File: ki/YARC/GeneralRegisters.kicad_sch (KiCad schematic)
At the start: 0 parts

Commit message: Ongoing development of registers and ALU
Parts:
- added U? (x8): 74LS670, symbol 74xx:74LS670
- added U? (x4): 74LS157, symbol 74xx:74LS157
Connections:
- new net: U?.16 (VCC), U?.16 (VCC), U?.16 (VCC)
- new net: U?.8 (GND), U?.8 (GND), U?.8 (GND)
- new net 333: U?.12 (~{Ew})
- new net 4444: U?.11 (~{Er})
- new net 55555: U?.4 (Rb)
- new net ALUOUT15: U?.14 (I0d)
- new net DW.15: U?.3 (D4)
- new net SRC2.15: U?.6 (Q4)
- new net SYSDATA15: U?.13 (I1d)
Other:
- note added: "REGISTER BANK 1"
- note added: "REGISTER BANK 2"
- note added: "REGISTER INPUT MUX"

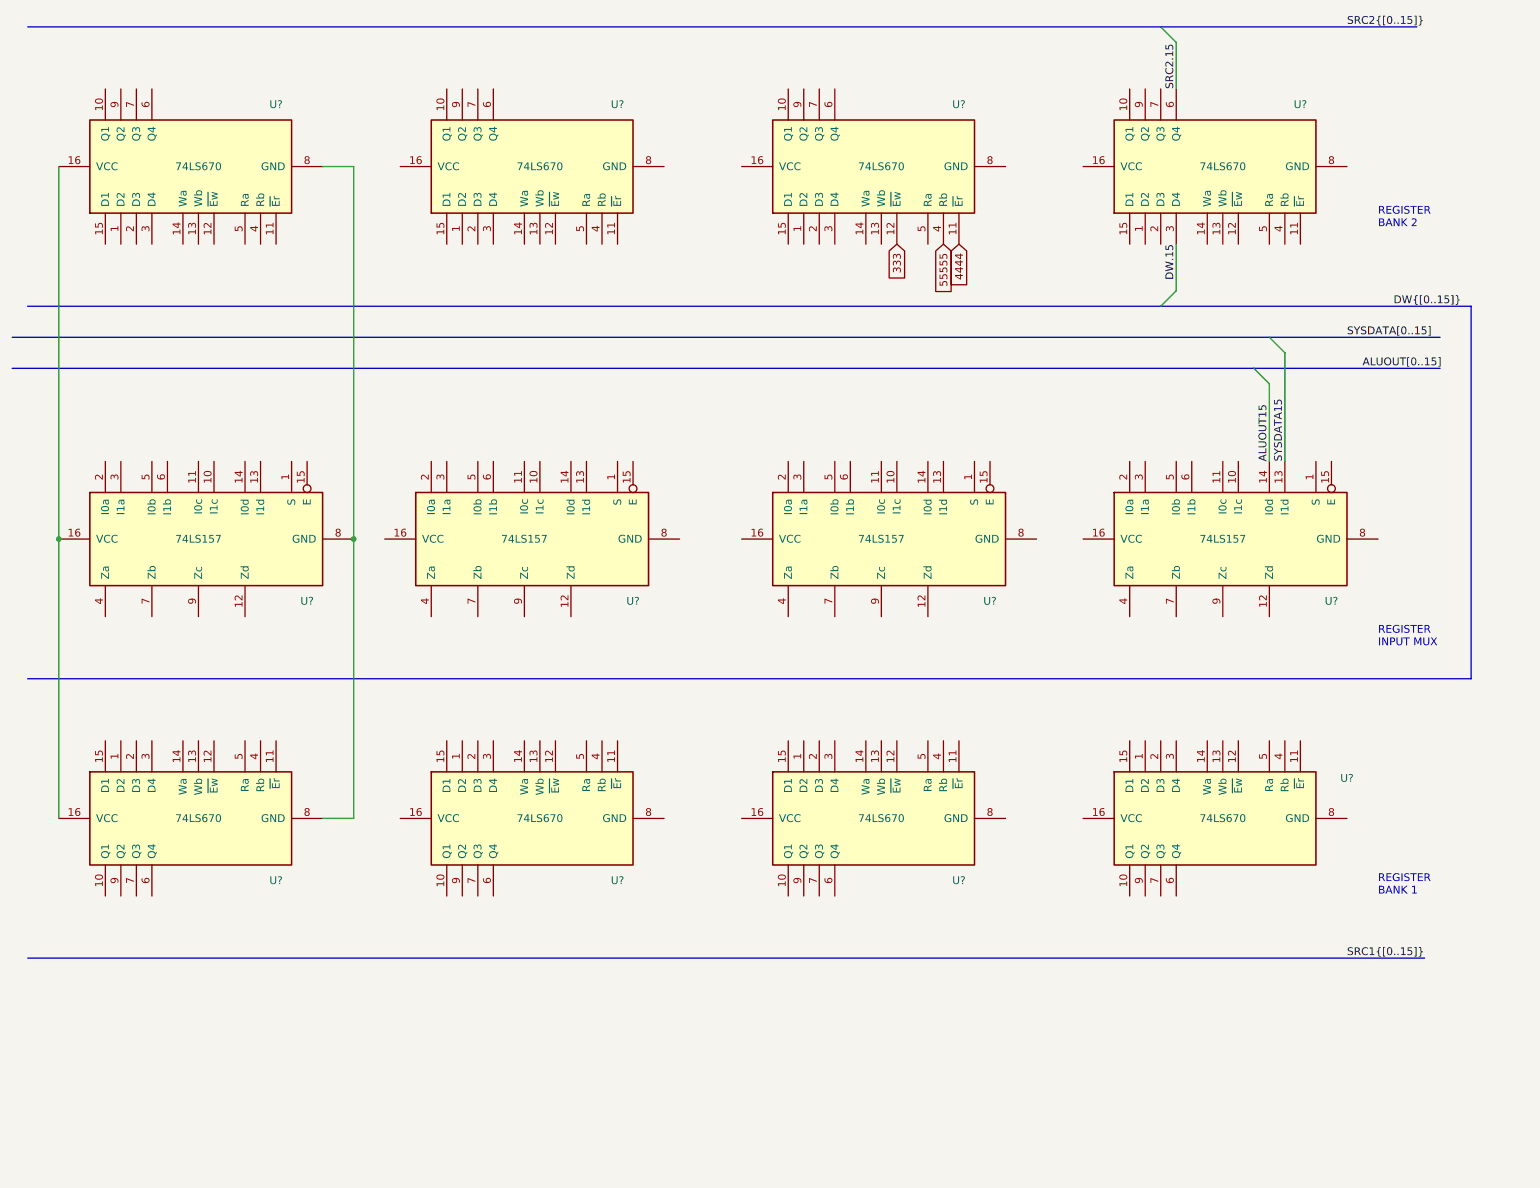
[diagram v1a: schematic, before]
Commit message: Expand ucode RAM test to 4 slices. Much work in KiCad.
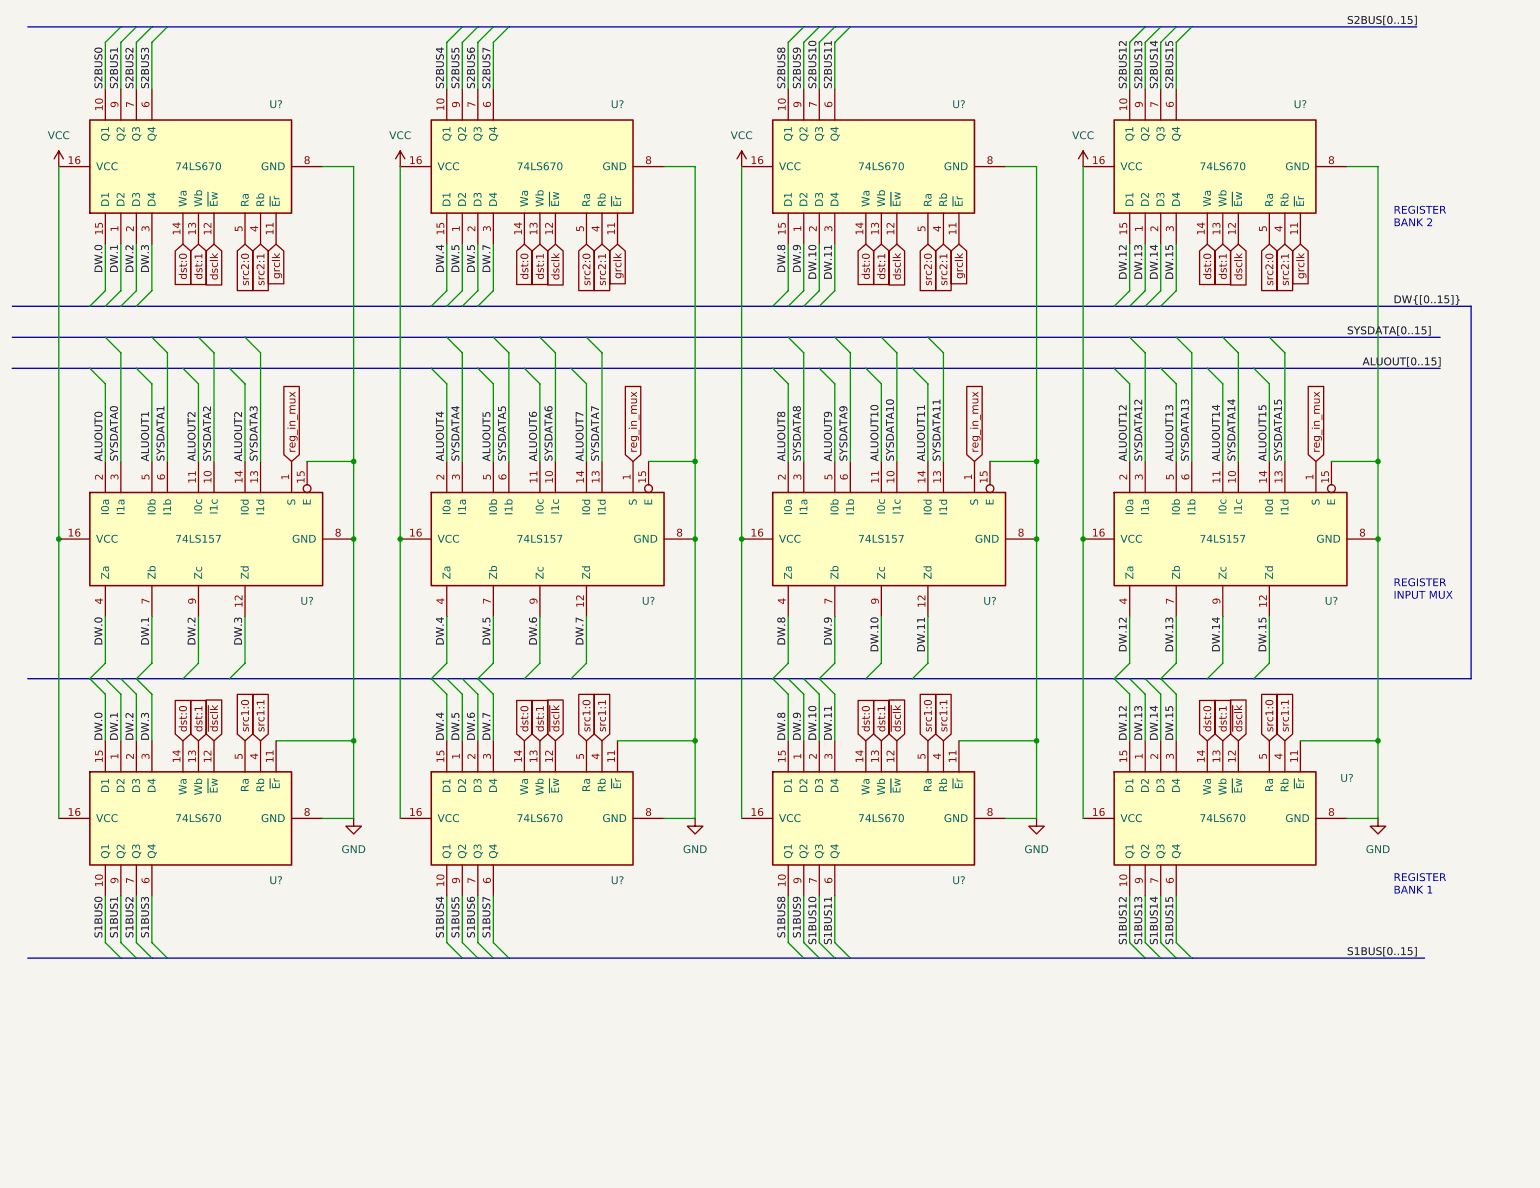
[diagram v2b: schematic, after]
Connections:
- net 333 is gone; now on net dsclk: U?.12 (~{Ew})
- net 4444 is gone; now on net grclk: U?.11 (~{Er})
- net 55555 is gone; now on net src2:1: U?.4 (Rb)
- net DW.15: now also U?.12 (Zd), U?.3 (D4)
- net DW.9: now reaches U?.1 (D2)
- net DW.9: now also U?.1 (D2), U?.7 (Zb)
- net S1BUS8: now reaches U?.10 (Q1)
- net GND: now reaches U?.11 (~{Er})
- net GND: now also U?.11 (~{Er}), U?.11 (~{Er}), U?.11 (~{Er}), U?.15 (E), U?.15 (E), U?.15 (E), U?.15 (E), U?.8 (GND), U?.8 (GND), U?.8 (GND), U?.8 (GND), U?.8 (GND), U?.8 (GND), U?.8 (GND), U?.8 (GND), U?.8 (GND), U?.8 (GND), U?.8 (GND), U?.8 (GND)
- net ~{dsclk}: now reaches U?.12 (~{Ew})
- net ~{dsclk}: now also U?.12 (~{Ew}), U?.12 (~{Ew}), U?.12 (~{Ew})
- net dst:1: now reaches U?.13 (Wb)
- net dst:1: now also U?.13 (Wb), U?.13 (Wb), U?.13 (Wb), U?.13 (Wb), U?.13 (Wb), U?.13 (Wb), U?.13 (Wb)
- net dst:0: now reaches U?.14 (Wa)
- net dst:0: now also U?.14 (Wa), U?.14 (Wa), U?.14 (Wa), U?.14 (Wa), U?.14 (Wa), U?.14 (Wa), U?.14 (Wa)
- net DW.8: now reaches U?.15 (D1)
- net DW.8: now also U?.15 (D1), U?.4 (Za)
- net VCC: now reaches U?.16 (VCC)
- net VCC: now also U?.16 (VCC), U?.16 (VCC), U?.16 (VCC), U?.16 (VCC), U?.16 (VCC), U?.16 (VCC), U?.16 (VCC), U?.16 (VCC), U?.16 (VCC), U?.16 (VCC), U?.16 (VCC)
- net DW.10: now reaches U?.2 (D3)
- net DW.10: now also U?.2 (D3), U?.9 (Zc)
- net DW.11: now reaches U?.3 (D4)
- net DW.11: now also U?.12 (Zd), U?.3 (D4)
- net src1:1: now reaches U?.4 (Rb)
- net src1:1: now also U?.4 (Rb), U?.4 (Rb), U?.4 (Rb)
- net src1:0: now reaches U?.5 (Ra)
- net src1:0: now also U?.5 (Ra), U?.5 (Ra), U?.5 (Ra)
- net S1BUS11: now reaches U?.6 (Q4)
- net S1BUS10: now reaches U?.7 (Q3)
- net S1BUS9: now reaches U?.9 (Q2)
- net DW.13: now reaches U?.1 (D2)
- net DW.13: now also U?.1 (D2), U?.7 (Zb)
- net S1BUS12: now reaches U?.10 (Q1)
- net DW.12: now reaches U?.15 (D1)
- net DW.12: now also U?.15 (D1), U?.4 (Za)
- net DW.14: now reaches U?.2 (D3)
- net DW.14: now also U?.2 (D3), U?.9 (Zc)
- net S1BUS15: now reaches U?.6 (Q4)
- net S1BUS14: now reaches U?.7 (Q3)
- net S1BUS13: now reaches U?.9 (Q2)
- net DW.5: now reaches U?.1 (D2)
- net DW.5: now also U?.1 (D2), U?.2 (D3), U?.7 (Zb)
- net S2BUS4: now reaches U?.10 (Q1)
- net grclk: now reaches U?.11 (~{Er})
- net grclk: now also U?.11 (~{Er}), U?.11 (~{Er})
- net dsclk: now reaches U?.12 (~{Ew})
- net dsclk: now also U?.12 (~{Ew}), U?.12 (~{Ew})
- net DW.4: now reaches U?.15 (D1)
- net DW.4: now also U?.15 (D1), U?.4 (Za)
- net DW.7: now reaches U?.3 (D4)
- net DW.7: now also U?.12 (Zd), U?.3 (D4)
- net src2:1: now reaches U?.4 (Rb)
- net src2:1: now also U?.4 (Rb), U?.4 (Rb)
- net src2:0: now reaches U?.5 (Ra)
- net src2:0: now also U?.5 (Ra), U?.5 (Ra), U?.5 (Ra)
- net S2BUS7: now reaches U?.6 (Q4)
- net S2BUS6: now reaches U?.7 (Q3)
- net S2BUS5: now reaches U?.9 (Q2)
- net reg_in_mux: now reaches U?.1 (S)
- net reg_in_mux: now also U?.1 (S), U?.1 (S), U?.1 (S)
- net SYSDATA10: now reaches U?.10 (I1c)
- net ALUOUT10: now reaches U?.11 (I0c)
- net SYSDATA11: now reaches U?.13 (I1d)
- net ALUOUT11: now reaches U?.14 (I0d)
- net ALUOUT8: now reaches U?.2 (I0a)
- net SYSDATA8: now reaches U?.3 (I1a)
- net ALUOUT9: now reaches U?.5 (I0b)
- net SYSDATA9: now reaches U?.6 (I1b)
- net SYSDATA2: now reaches U?.10 (I1c)
- net ALUOUT2: now reaches U?.11 (I0c)
- net ALUOUT2: now also U?.14 (I0d)
- net DW.3: now reaches U?.12 (Zd)
- net DW.3: now also U?.3 (D4), U?.3 (D4)
- net SYSDATA3: now reaches U?.13 (I1d)
- net ALUOUT0: now reaches U?.2 (I0a)
- net SYSDATA0: now reaches U?.3 (I1a)
- net DW.0: now reaches U?.4 (Za)
- net DW.0: now also U?.15 (D1), U?.15 (D1)
- net ALUOUT1: now reaches U?.5 (I0b)
- net SYSDATA1: now reaches U?.6 (I1b)
- net DW.1: now reaches U?.7 (Zb)
- net DW.1: now also U?.1 (D2), U?.1 (D2)
- net DW.2: now reaches U?.9 (Zc)
- net DW.2: now also U?.2 (D3), U?.2 (D3)
- net S2BUS12: now reaches U?.10 (Q1)
- net S2BUS14: now reaches U?.7 (Q3)
- net S2BUS13: now reaches U?.9 (Q2)
- net S1BUS0: now reaches U?.10 (Q1)
- net S1BUS3: now reaches U?.6 (Q4)
- net S1BUS2: now reaches U?.7 (Q3)
- net S1BUS1: now reaches U?.9 (Q2)
- net S1BUS4: now reaches U?.10 (Q1)
- net DW.6: now reaches U?.2 (D3)
- net DW.6: now also U?.9 (Zc)
- net S1BUS7: now reaches U?.6 (Q4)
- net S1BUS6: now reaches U?.7 (Q3)
- net S1BUS5: now reaches U?.9 (Q2)
- net SYSDATA6: now reaches U?.10 (I1c)
- net ALUOUT6: now reaches U?.11 (I0c)
- net SYSDATA7: now reaches U?.13 (I1d)
- net ALUOUT7: now reaches U?.14 (I0d)
- net ALUOUT4: now reaches U?.2 (I0a)
- net SYSDATA4: now reaches U?.3 (I1a)
- net ALUOUT5: now reaches U?.5 (I0b)
- net SYSDATA5: now reaches U?.6 (I1b)
- net S2BUS8: now reaches U?.10 (Q1)
- net S2BUS11: now reaches U?.6 (Q4)
- net S2BUS10: now reaches U?.7 (Q3)
- net S2BUS9: now reaches U?.9 (Q2)
- net S2BUS0: now reaches U?.10 (Q1)
- net S2BUS3: now reaches U?.6 (Q4)
- net S2BUS2: now reaches U?.7 (Q3)
- net S2BUS1: now reaches U?.9 (Q2)
- net SYSDATA14: now reaches U?.10 (I1c)
- net ALUOUT14: now reaches U?.11 (I0c)
- net ALUOUT12: now reaches U?.2 (I0a)
- net SYSDATA12: now reaches U?.3 (I1a)
- net ALUOUT13: now reaches U?.5 (I0b)
- net SYSDATA13: now reaches U?.6 (I1b)
- net SRC2.15 renamed S2BUS15
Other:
- moved on the sheet: U?

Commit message: Assign part labels (U-numbers) in KiCad and start adding them to Fritzing layouts
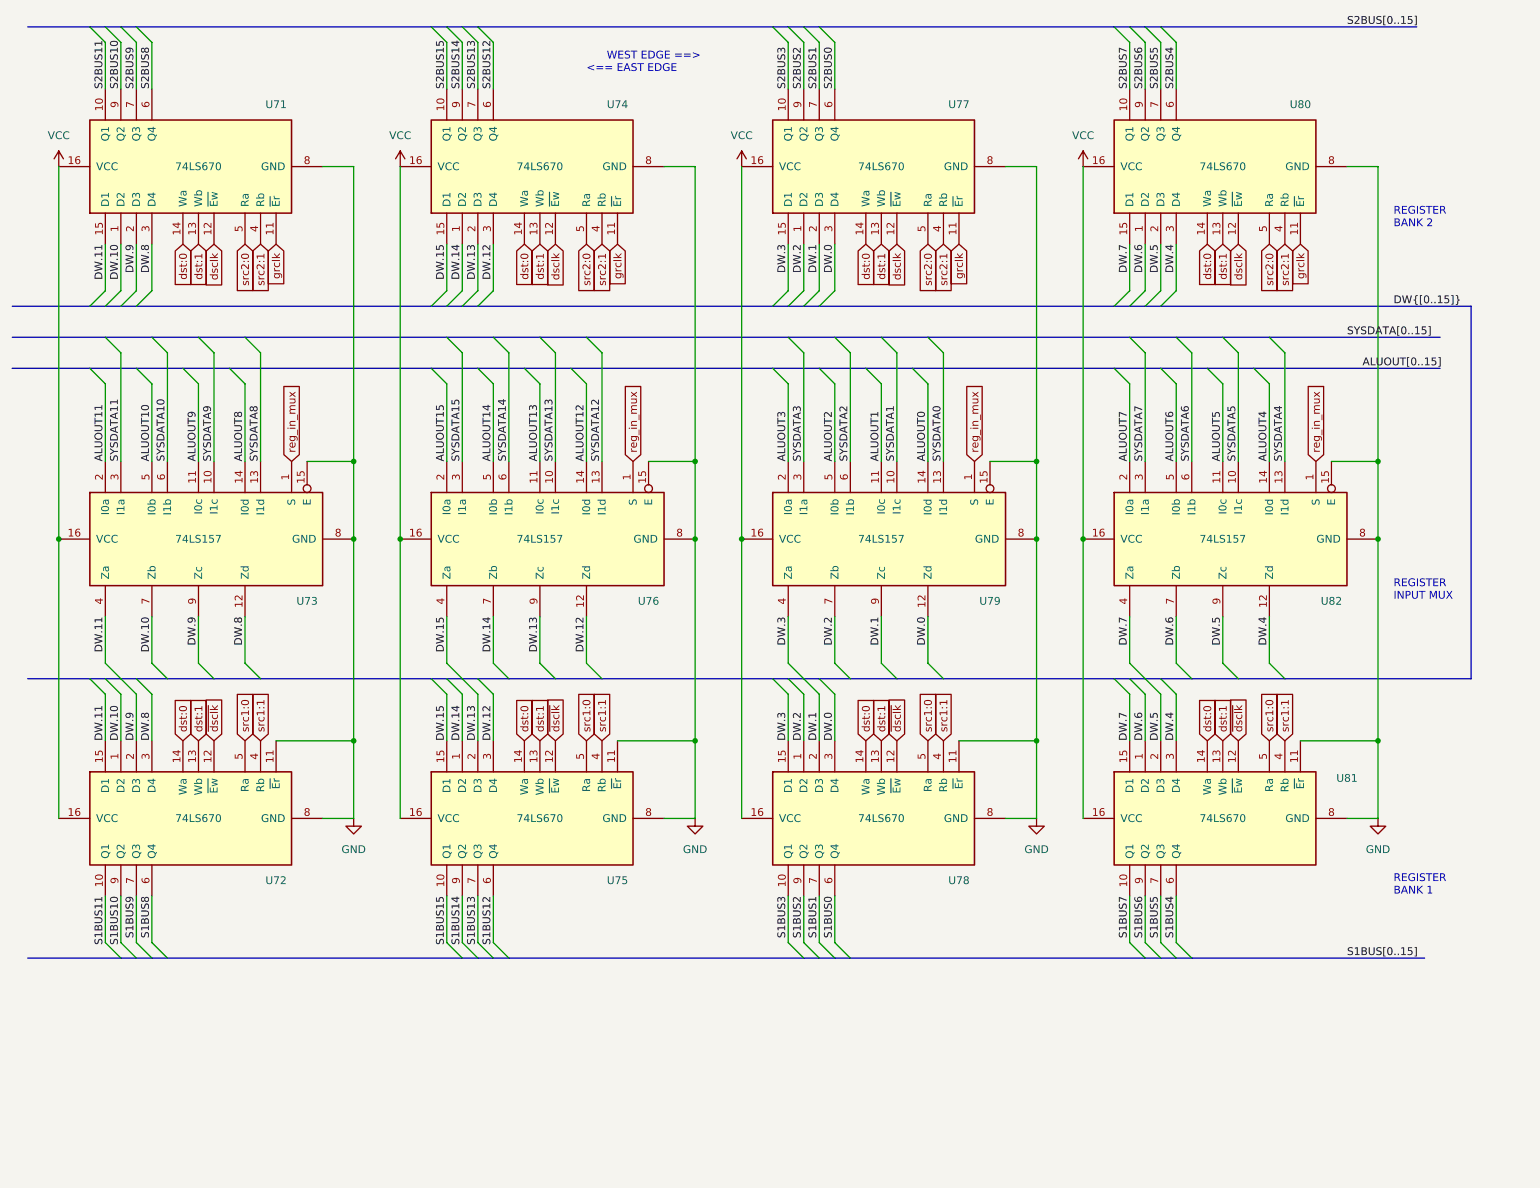
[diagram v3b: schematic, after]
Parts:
- gave numbers to parts that had none: 12
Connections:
- net ALUOUT0: now also U79.14 (I0d); no longer U73.2 (I0a)
- net ALUOUT1: now also U79.11 (I0c); no longer U73.5 (I0b)
- net ALUOUT10: now also U73.5 (I0b); no longer U79.11 (I0c)
- net ALUOUT11: now also U73.2 (I0a); no longer U79.14 (I0d)
- net ALUOUT12: now also U76.14 (I0d); no longer U82.2 (I0a)
- net ALUOUT13: now also U76.11 (I0c); no longer U82.5 (I0b)
- net ALUOUT14: now also U76.5 (I0b); no longer U82.11 (I0c)
- net ALUOUT15: now also U76.2 (I0a); no longer U82.14 (I0d)
- net ALUOUT2: now also U79.5 (I0b); no longer U73.11 (I0c), U73.14 (I0d)
- net ALUOUT4: now also U82.14 (I0d); no longer U76.2 (I0a)
- net ALUOUT5: now also U82.11 (I0c); no longer U76.5 (I0b)
- net ALUOUT6: now also U82.5 (I0b); no longer U76.11 (I0c)
- net ALUOUT7: now also U82.2 (I0a); no longer U76.14 (I0d)
- net ALUOUT8: now also U73.14 (I0d); no longer U79.2 (I0a)
- net ALUOUT9: now also U73.11 (I0c); no longer U79.5 (I0b)
- net DW.0: now also U77.3 (D4), U78.3 (D4), U79.12 (Zd); no longer U71.15 (D1), U72.15 (D1), U73.4 (Za)
- net DW.1: now also U77.2 (D3), U78.2 (D3), U79.9 (Zc); no longer U71.1 (D2), U72.1 (D2), U73.7 (Zb)
- net DW.10: now also U71.1 (D2), U72.1 (D2), U73.7 (Zb); no longer U77.2 (D3), U78.2 (D3), U79.9 (Zc)
- net DW.11: now also U71.15 (D1), U72.15 (D1), U73.4 (Za); no longer U77.3 (D4), U78.3 (D4), U79.12 (Zd)
- net DW.12: now also U74.3 (D4), U75.3 (D4), U76.12 (Zd); no longer U80.15 (D1), U81.15 (D1), U82.4 (Za)
- net DW.13: now also U74.2 (D3), U75.2 (D3), U76.9 (Zc); no longer U80.1 (D2), U81.1 (D2), U82.7 (Zb)
- net DW.14: now also U74.1 (D2), U75.1 (D2), U76.7 (Zb); no longer U80.2 (D3), U81.2 (D3), U82.9 (Zc)
- net DW.15: now also U74.15 (D1), U75.15 (D1), U76.4 (Za); no longer U80.3 (D4), U81.3 (D4), U82.12 (Zd)
- net DW.2: now also U77.1 (D2), U78.1 (D2), U79.7 (Zb); no longer U71.2 (D3), U72.2 (D3), U73.9 (Zc)
- net DW.3: now also U77.15 (D1), U78.15 (D1), U79.4 (Za); no longer U71.3 (D4), U72.3 (D4), U73.12 (Zd)
- net DW.4: now also U80.3 (D4), U81.3 (D4), U82.12 (Zd); no longer U74.15 (D1), U75.15 (D1), U76.4 (Za)
- net DW.5: now also U80.2 (D3), U81.2 (D3), U82.9 (Zc); no longer U74.1 (D2), U74.2 (D3), U75.1 (D2), U76.7 (Zb)
- net DW.6: now also U80.1 (D2), U81.1 (D2), U82.7 (Zb); no longer U75.2 (D3), U76.9 (Zc)
- net DW.7: now also U80.15 (D1), U81.15 (D1), U82.4 (Za); no longer U74.3 (D4), U75.3 (D4), U76.12 (Zd)
- net DW.8: now also U71.3 (D4), U72.3 (D4), U73.12 (Zd); no longer U77.15 (D1), U78.15 (D1), U79.4 (Za)
- net DW.9: now also U71.2 (D3), U72.2 (D3), U73.9 (Zc); no longer U77.1 (D2), U78.1 (D2), U79.7 (Zb)
- net S1BUS0: now also U78.6 (Q4); no longer U72.10 (Q1)
- net S1BUS1: now also U78.7 (Q3); no longer U72.9 (Q2)
- net S1BUS10: now also U72.9 (Q2); no longer U78.7 (Q3)
- net S1BUS11: now also U72.10 (Q1); no longer U78.6 (Q4)
- net S1BUS12: now also U75.6 (Q4); no longer U81.10 (Q1)
- net S1BUS13: now also U75.7 (Q3); no longer U81.9 (Q2)
- net S1BUS14: now also U75.9 (Q2); no longer U81.7 (Q3)
- net S1BUS15: now also U75.10 (Q1); no longer U81.6 (Q4)
- net S1BUS2: now also U78.9 (Q2); no longer U72.7 (Q3)
- net S1BUS3: now also U78.10 (Q1); no longer U72.6 (Q4)
- net S1BUS4: now also U81.6 (Q4); no longer U75.10 (Q1)
- net S1BUS5: now also U81.7 (Q3); no longer U75.9 (Q2)
- net S1BUS6: now also U81.9 (Q2); no longer U75.7 (Q3)
- net S1BUS7: now also U81.10 (Q1); no longer U75.6 (Q4)
- net S1BUS8: now also U72.6 (Q4); no longer U78.10 (Q1)
- net S1BUS9: now also U72.7 (Q3); no longer U78.9 (Q2)
- net S2BUS0: now also U77.6 (Q4); no longer U71.10 (Q1)
- net S2BUS1: now also U77.7 (Q3); no longer U71.9 (Q2)
- net S2BUS10: now also U71.9 (Q2); no longer U77.7 (Q3)
- net S2BUS11: now also U71.10 (Q1); no longer U77.6 (Q4)
- net S2BUS12: now also U74.6 (Q4); no longer U80.10 (Q1)
- net S2BUS13: now also U74.7 (Q3); no longer U80.9 (Q2)
- net S2BUS14: now also U74.9 (Q2); no longer U80.7 (Q3)
- net S2BUS15: now also U74.10 (Q1); no longer U80.6 (Q4)
- net S2BUS2: now also U77.9 (Q2); no longer U71.7 (Q3)
- net S2BUS3: now also U77.10 (Q1); no longer U71.6 (Q4)
- net S2BUS4: now also U80.6 (Q4); no longer U74.10 (Q1)
- net S2BUS5: now also U80.7 (Q3); no longer U74.9 (Q2)
- net S2BUS6: now also U80.9 (Q2); no longer U74.7 (Q3)
- net S2BUS7: now also U80.10 (Q1); no longer U74.6 (Q4)
- net S2BUS8: now also U71.6 (Q4); no longer U77.10 (Q1)
- net S2BUS9: now also U71.7 (Q3); no longer U77.9 (Q2)
- net SYSDATA0: now also U79.13 (I1d); no longer U73.3 (I1a)
- net SYSDATA1: now also U79.10 (I1c); no longer U73.6 (I1b)
- net SYSDATA10: now also U73.6 (I1b); no longer U79.10 (I1c)
- net SYSDATA11: now also U73.3 (I1a); no longer U79.13 (I1d)
- net SYSDATA12: now also U76.13 (I1d); no longer U82.3 (I1a)
- net SYSDATA13: now also U76.10 (I1c); no longer U82.6 (I1b)
- net SYSDATA14: now also U76.6 (I1b); no longer U82.10 (I1c)
- net SYSDATA15: now also U76.3 (I1a); no longer U82.13 (I1d)
- net SYSDATA2: now also U79.6 (I1b); no longer U73.10 (I1c)
- net SYSDATA3: now also U79.3 (I1a); no longer U73.13 (I1d)
- net SYSDATA4: now also U82.13 (I1d); no longer U76.3 (I1a)
- net SYSDATA5: now also U82.10 (I1c); no longer U76.6 (I1b)
- net SYSDATA6: now also U82.6 (I1b); no longer U76.10 (I1c)
- net SYSDATA7: now also U82.3 (I1a); no longer U76.13 (I1d)
- net SYSDATA8: now also U73.13 (I1d); no longer U79.3 (I1a)
- net SYSDATA9: now also U73.10 (I1c); no longer U79.6 (I1b)
- new net ALUOUT3: U79.2 (I0a)
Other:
- note added: "WEST EDGE ==> <== EAST EDGE"
